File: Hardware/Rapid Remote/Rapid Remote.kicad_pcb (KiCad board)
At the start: 2 copper layers, 27.9 x 38.1 mm, 4 parts

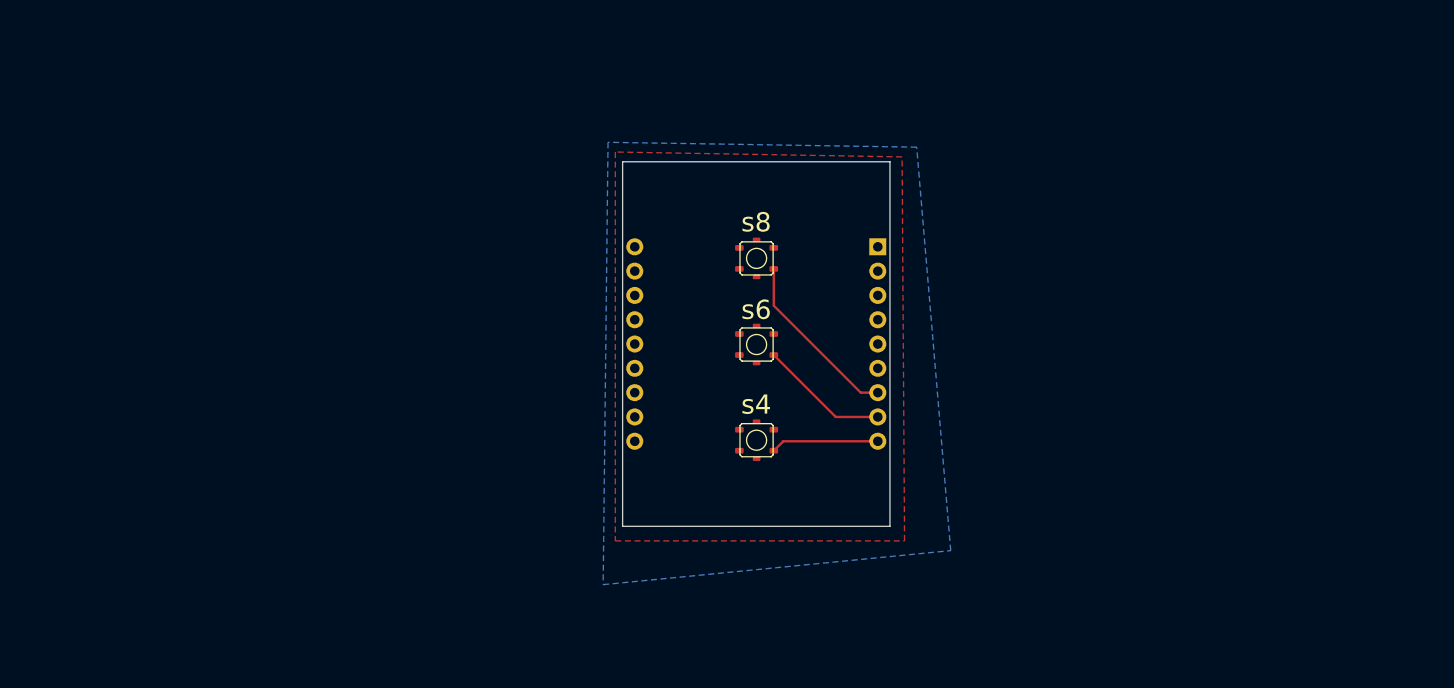
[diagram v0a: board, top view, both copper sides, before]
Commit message: added initial remote code and more layout for remote
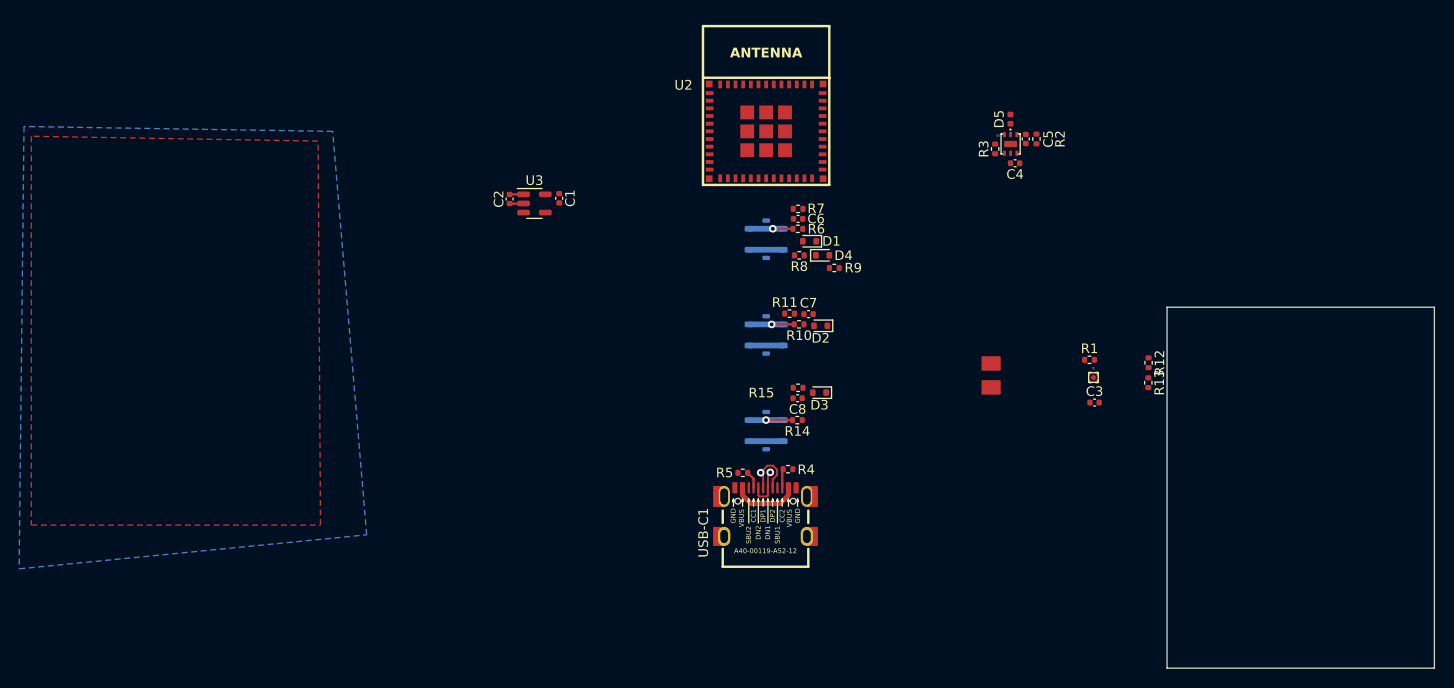
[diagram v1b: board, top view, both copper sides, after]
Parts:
- removed U1: ~, Personal:ESP32-C3-DevKit
- added C1: 1u, Capacitor_SMD:C_0402_1005Metric, F.Cu at (129.0, 81.8)
- added C2: 1u, Capacitor_SMD:C_0402_1005Metric, F.Cu at (123.8, 81.9)
- added C3: 0.1u, Capacitor_SMD:C_0402_1005Metric, F.Cu at (185.0, 103.1)
- added C4: 10u, Capacitor_SMD:C_0402_1005Metric, F.Cu at (176.7, 78.1)
- added C5: 1u, Capacitor_SMD:C_0402_1005Metric, F.Cu at (177.8, 75.6)
- added C6: 1u, Capacitor_SMD:C_0402_1005Metric, F.Cu at (154.0, 83.9)
- added C7: 1u, Capacitor_SMD:C_0402_1005Metric, F.Cu at (155.1, 93.9)
- added C8: 1u, Capacitor_SMD:C_0402_1005Metric, F.Cu at (153.9, 102.7)
- added D1: 1N4148WT, Diode_SMD:D_SOD-523, F.Cu at (155.2, 86.3)
- added D2: 1N4148WT, Diode_SMD:D_SOD-523, F.Cu at (156.3, 95.1)
- added D3: 1N4148WT, Diode_SMD:D_SOD-523, F.Cu at (156.2, 102.1)
- added D4: 1N4148WT, Diode_SMD:D_SOD-523, F.Cu at (156.5, 87.8)
- added D5: LED, LED_SMD:LED_0402_1005Metric, F.Cu at (176.2, 73.5)
- added R1: 100R, Resistor_SMD:R_0402_1005Metric, F.Cu at (184.4, 98.7)
- added R10: 1k, Resistor_SMD:R_0402_1005Metric, F.Cu at (154.1, 95.0)
- added R11: 10k, Resistor_SMD:R_0402_1005Metric, F.Cu at (153.1, 93.9)
- added R12: 1M, Resistor_SMD:R_0402_1005Metric, F.Cu at (190.6, 99.0)
- added R13: 250k, Resistor_SMD:R_0402_1005Metric, F.Cu at (190.6, 101.1)
- added R14: 1k, Resistor_SMD:R_0402_1005Metric, F.Cu at (153.9, 105.0)
- added R15: 10k, Resistor_SMD:R_0402_1005Metric, F.Cu at (154.0, 101.6)
- added R2: 1k, Resistor_SMD:R_0402_1005Metric, F.Cu at (178.9, 75.6)
- added R3: 47.5k, Resistor_SMD:R_0402_1005Metric, F.Cu at (174.6, 76.6)
- added R4: 5k1, Resistor_SMD:R_0402_1005Metric, F.Cu at (152.9, 110.1)
- added R5: 5k1, Resistor_SMD:R_0402_1005Metric, F.Cu at (148.2, 110.5)
- added R6: 1k, Resistor_SMD:R_0402_1005Metric, F.Cu at (153.9, 85.0)
- added R7: 10k, Resistor_SMD:R_0402_1005Metric, F.Cu at (154.0, 82.9)
- added R8: 10k, Resistor_SMD:R_0402_1005Metric, F.Cu at (154.1, 87.8)
- added R9: 1M, Resistor_SMD:R_0402_1005Metric, F.Cu at (157.8, 89.1)
- added TP1: TP/SP-1.5X2.0, Personal:SOLDERPAD_1.5X2.0, F.Cu at (174.1, 99.1)
- added TP2: TP/SP-1.5X2.0, Personal:SOLDERPAD_1.5X2.0, F.Cu at (174.1, 101.6)
- added U2: ESP32-C3-MINI-1-N4, Personal:ESP32-­C3-­MINI­-1, F.Cu at (150.6, 74.8)
- added U3: MIC5504-3.3YM5, Package_TO_SOT_SMD:SOT-23-5, F.Cu at (126.4, 82.3)
- added U4: XB6042I2SV, Personal:TDFN4, F.Cu at (184.8, 100.5)
- added U5: WS4518D, Personal:DFN-6, F.Cu at (176.2, 76.1)
- added USB-C1: USB-C-16P-F(A40-00119-A52-12), Personal:USB2.0_TYPE-C(A40-00119-A52-12), F.Cu at (150.6, 116.0)
- s4, s6, s8: moved to B.Cu
- moved s8 2.24 mm to (150.6, 86.1), turned to 180 degrees
- moved s4 1.41 mm to (150.6, 106.1), turned to 180 degrees
- moved s6 1.41 mm to (150.6, 96.1), turned to 180 degrees
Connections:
- s4 pad P1: +3V3 -> Net-(s4-1)
- s4 pad P2: unconnected-(s4-2-PadP2) -> Net-(s4-1)
- s4 pad P3: unconnected-(s4-3-PadP3) -> +BATT
- s4 pad P4: Net-(U1-GPIO6) -> +BATT
- s6 pad P1: +3V3 -> Net-(s6-1)
- s6 pad P2: unconnected-(s6-2-PadP2) -> Net-(s6-1)
- s6 pad P3: unconnected-(s6-3-PadP3) -> +BATT
- s6 pad P4: Net-(U1-GPIO5) -> +BATT
- s8 pad P1: +3V3 -> Net-(s8-1)
- s8 pad P2: unconnected-(s8-2-PadP2) -> Net-(s8-1)
- s8 pad P3: unconnected-(s8-3-PadP3) -> +BATT
- s8 pad P4: Net-(U1-GPIO4) -> +BATT
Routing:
- net Net-(U1-GPIO4): track 18.5 -> 0.00 mm
- net Net-(U1-GPIO5): track 13.5 -> 0.00 mm
- net +BATT: track 0.00 -> 12.3 mm
- net Net-(U1-GPIO6): track 11.3 -> 0.00 mm
- net +5V: track 0.00 -> 7.39 mm
- net Net-(s4-1): track 0.00 -> 6.37 mm, vias 0 -> 1
- net USB_D+: track 0.00 -> 5.98 mm, vias 0 -> 1
- net Net-(s6-1): track 0.00 -> 5.96 mm, vias 0 -> 1
- net Net-(s8-1): track 0.00 -> 5.71 mm, vias 0 -> 1
- net USB_D-: track 0.00 -> 4.40 mm, vias 0 -> 1
- net Net-(USB-C1-CC2): track 0.00 -> 1.99 mm
- net Net-(USB-C1-CC1): track 0.00 -> 1.83 mm
- net GND: track 0.00 -> 1.46 mm
- added copper zone on F.Cu, net GND
- removed copper zone on F.Cu, net +3V3
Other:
- board size 27.9 x 38.1 mm -> 27.9 x 37.7 mm

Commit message: added battery and code for remote
Added a cr2032 battery for power and finished the layout and programming of the remote
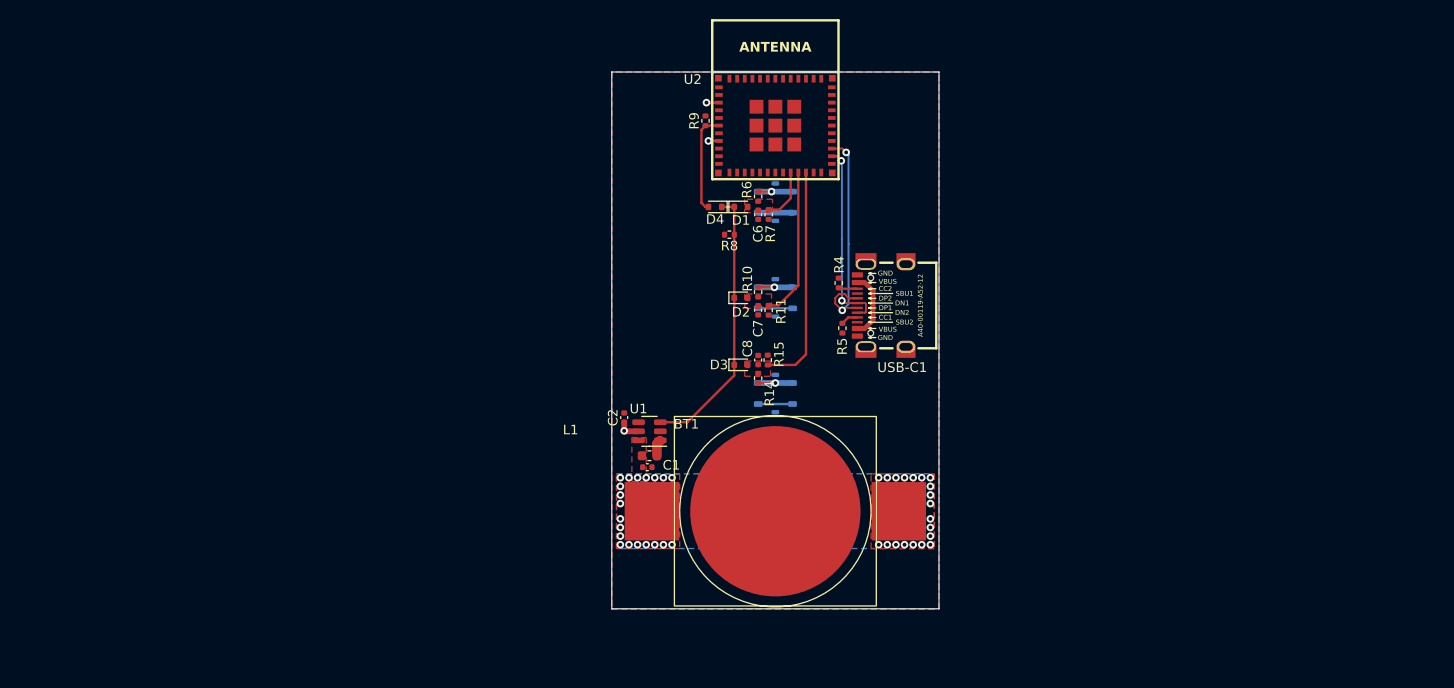
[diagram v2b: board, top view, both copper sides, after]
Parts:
- removed C3: 0.1u, Capacitor_SMD:C_0402_1005Metric
- removed C4: 10u, Capacitor_SMD:C_0402_1005Metric
- removed C5: 1u, Capacitor_SMD:C_0402_1005Metric
- removed D5: LED, LED_SMD:LED_0402_1005Metric
- removed R1: 100R, Resistor_SMD:R_0402_1005Metric
- removed R12: 1M, Resistor_SMD:R_0402_1005Metric
- removed R13: 250k, Resistor_SMD:R_0402_1005Metric
- removed R2: 1k, Resistor_SMD:R_0402_1005Metric
- removed R3: 47.5k, Resistor_SMD:R_0402_1005Metric
- removed TP1, TP2: TP/SP-1.5X2.0, Personal:SOLDERPAD_1.5X2.0
- removed U3: MIC5504-3.3YM5, Package_TO_SOT_SMD:SOT-23-5
- removed U4: XB6042I2SV, Personal:TDFN4
- removed U5: WS4518D, Personal:DFN-6
- added BT1: Battery_Cell, personal:MY-2032-04, F.Cu at (151.6, 114.5)
- added L1: 4.7u, Inductor_SMD:L_0603_1608Metric, F.Cu at (138.4, 108.7)
- added U1: ~, Package_TO_SOT_SMD:SOT-23-6, F.Cu at (138.4, 106.2)
- C1, C2: value 1u -> 10u
- moved C1 29.6 mm to (138.2, 109.9), turned to 0 degrees
- moved USB-C1 26.7 mm to (164.1, 93.0), turned to 0 degrees
- moved C2 25.8 mm to (135.8, 104.7), turned to 90 degrees
- moved R9 20.4 mm to (144.3, 73.7), turned to 90 degrees
- moved R4 20.2 mm to (158.2, 90.6), turned to 90 degrees
- moved R5 18.4 mm to (158.6, 95.4), turned to -90 degrees
- moved D4 12.3 mm to (145.3, 82.7), turned to 180 degrees
- moved D2 8.83 mm to (148.0, 92.2), turned to 0 degrees
- moved D3 8.71 mm to (148.0, 99.2), turned to 0 degrees
- moved D1 8.01 mm to (148.0, 82.7), turned to 0 degrees
- moved R8 7.61 mm to (146.8, 85.6)
- moved R14 6.00 mm to (149.8, 100.6), turned to -90 degrees
- moved C8 5.74 mm to (149.8, 98.7), turned to 90 degrees
- moved R10 5.45 mm to (149.8, 91.6), turned to 90 degrees
- moved R6 5.36 mm to (149.8, 81.6), turned to 90 degrees
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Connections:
- C1 pad 1: +3V3 -> +3V0
- C2 pad 1: +BATT -> +3V3
- U2 pad 18: ADC -> unconnected-(U2-IO4/GPIO4/ADC1_CH4/FSPIHD/MTMS-Pad18)
- U2 pad 20: 4S -> 8S
- U2 pad 22: 8S -> 4S
- s4 pad P3: +BATT -> +3V3
- s4 pad P4: +BATT -> +3V3
- s6 pad P3: +BATT -> +3V3
- s6 pad P4: +BATT -> +3V3
- s8 pad P3: +BATT -> +3V3
- s8 pad P4: +BATT -> +3V3
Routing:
- net EN_LDO: track 0.00 -> 28.7 mm
- net 4S: track 0.00 -> 23.5 mm
- net USB_D+: track 5.98 -> 24.5 mm, vias 1 -> 2
- net USB_D-: track 4.40 -> 20.2 mm, vias 1 -> 2
- net 6S: track 0.00 -> 15.8 mm
- net +3V3: track 0.07 -> 15.6 mm, vias 0 -> 3
- net +BATT: track 12.3 -> 0.00 mm
- net LATCH: track 0.00 -> 10.5 mm
- net 8S: track 0.00 -> 5.49 mm
- net Net-(U1-SW): track 0.00 -> 1.97 mm
- net GND: track 1.46 -> 0.00 mm
- net Net-(s4-1): track 6.37 -> 5.40 mm
- net Net-(s8-1): track 5.71 -> 5.00 mm
- net Net-(s6-1): track 5.96 -> 5.30 mm
- net +3V0: vias 0 -> 40
- added copper zone on B.Cu, net +3V0
- added copper zone on F.Cu, net +3V0
- added copper zone on B.Cu, net +3V3
- added copper zone on F.Cu, net 4S
- added copper zone on F.Cu, net 6S
- added copper zone on F.Cu, net 8S
- removed copper zone on B.Cu, net GND
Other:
- board size 27.9 x 37.7 mm -> 34.2 x 56.1 mm
- board text added: "Rapid Training Box Remote © 2023 Thomas Whyte-Venables Rev. B"

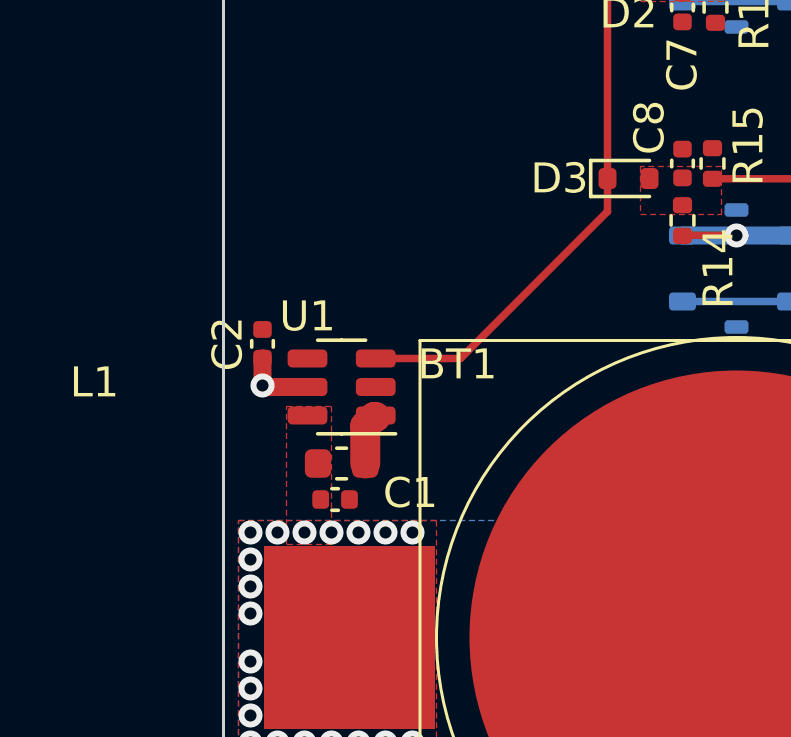
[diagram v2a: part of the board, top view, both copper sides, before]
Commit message: changed to 0603 capacitors
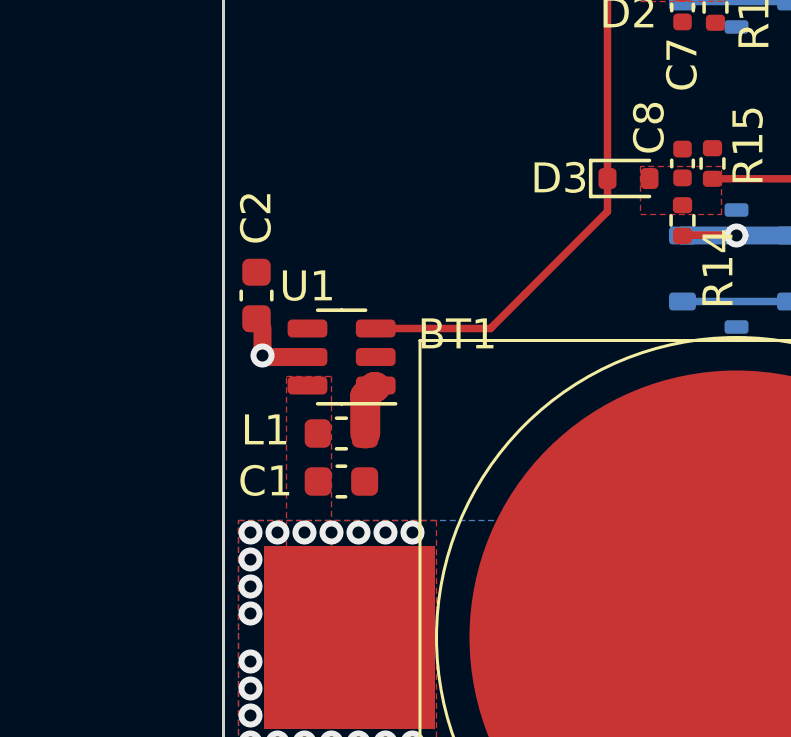
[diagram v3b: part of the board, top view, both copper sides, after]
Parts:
- C1, C2: footprint Capacitor_SMD:C_0402_1005Metric -> Capacitor_SMD:C_0603_1608Metric
- moved C2 1.62 mm to (135.6, 103.1)
- moved L1 1.00 mm to (138.4, 107.7)
- moved U1 1.00 mm to (138.4, 105.2)
- moved C1 0.64 mm to (138.4, 109.3)
